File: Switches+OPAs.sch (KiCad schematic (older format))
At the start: 23 parts, among them J15 Screw_Terminal_01x03, SW1 SW_Rotary2x6, SW2 SW_Rotary2x6, SW3 SW_Rotary2x6, SW4 SW_Rotary2x6, SW5 SW_Rotary2x6, SW6 SW_Rotary2x6, U1 TL072, U2 TL072, U3 TL072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

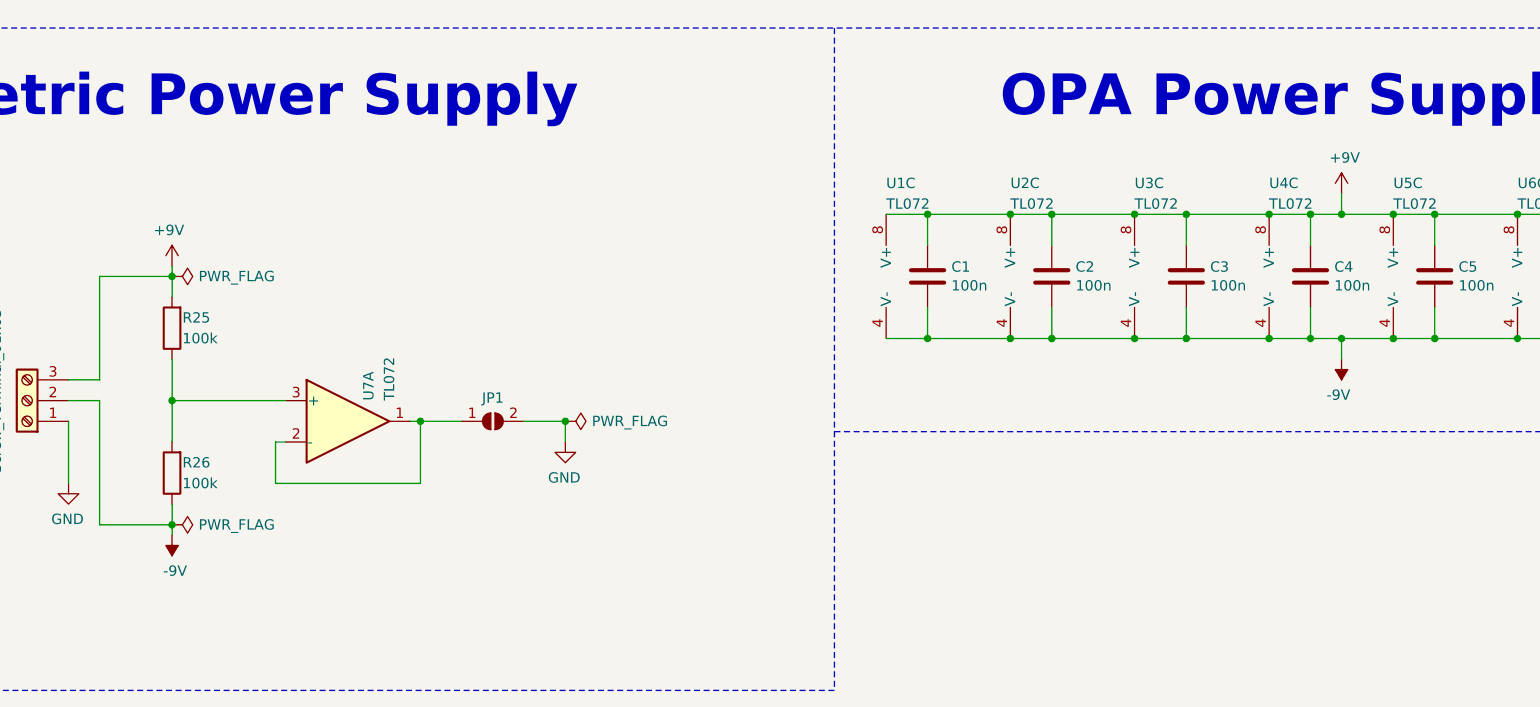
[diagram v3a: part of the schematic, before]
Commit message: added new attributes MF, MFN, Mouser, Digi-Key, RS-Online, Infopage, datasheet | bill of material (BOM) created | infobox updated | added AudioBürokrat logo on silkscreen
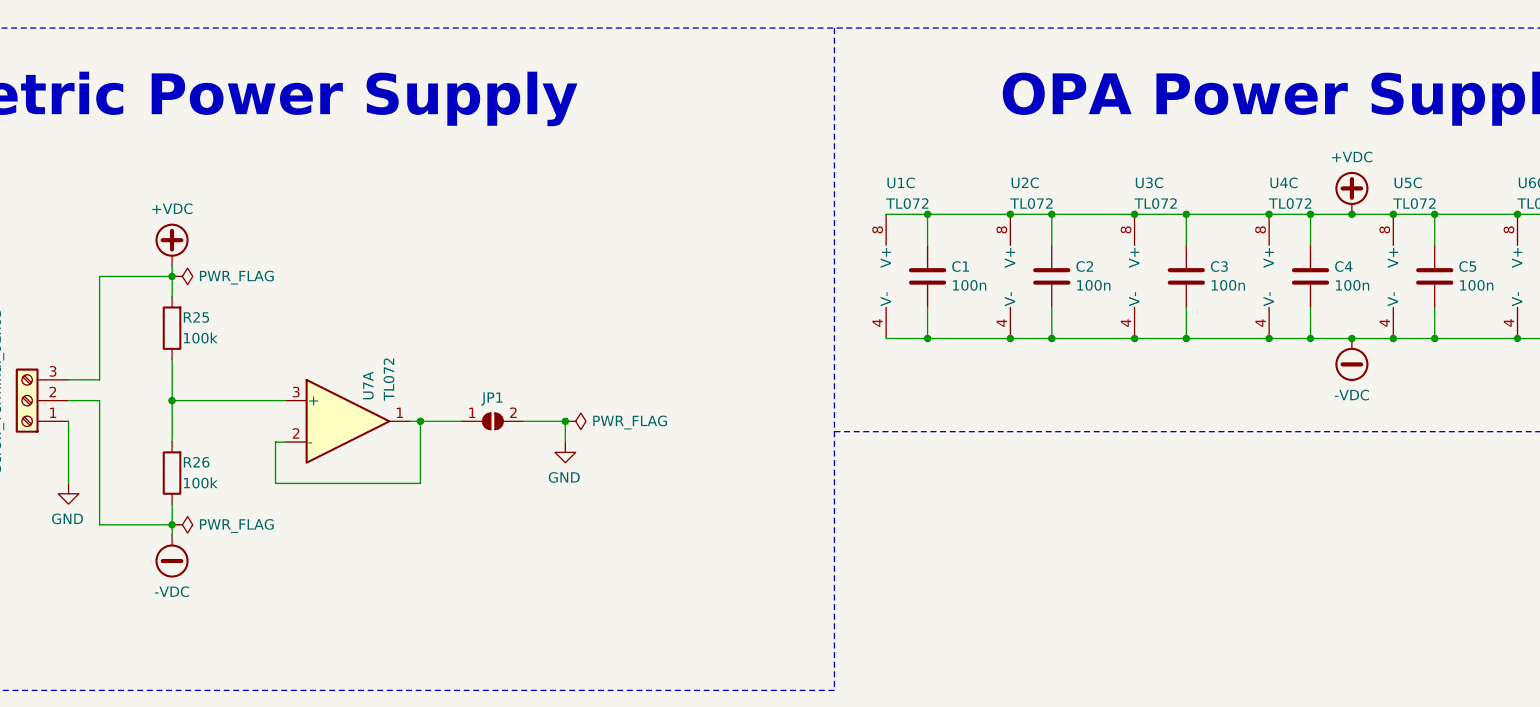
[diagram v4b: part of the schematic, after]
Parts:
- C1, C2, C3, C4, C5, C6: Digi-Key (none) -> 311-1779-1-ND; Infopage (none) -> —; MF (none) -> Yageo; MFN (none) -> CC0603JRX7R9BB104; Mouser (none) -> 603-CC603JRX7R9BB104; RS-Online (none) -> 200-6519
- J15: Digi-Key (none) -> 732-2029-ND; Infopage (none) -> https://www.we-online.de/katalog/de/TBL_5_00_102_6911027100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; MF (none) -> Wuerth; MFN (none) -> 691102710003; Mouser (none) -> 710-691102710003; RS-Online (none) -> 691102710003
- JP1: Digi-Key (none) -> —; Infopage (none) -> —; MF (none) -> —; MFN (none) -> —; Mouser (none) -> —; RS-Online (none) -> —
- R25, R26: Digi-Key (none) -> 541-3950-1-ND; Infopage (none) -> —; MF (none) -> Vishay; MFN (none) -> CRCW0603100KFKEAC; Mouser (none) -> 71-CRCW0603100KFKEAC; RS-Online (none) -> 820-6745
- SW1, SW2, SW3, SW4, SW5, SW6: Digi-Key (none) -> —; Infopage (none) -> https://lorlinelectronics.co.uk/product/ck; MF (none) -> Lorlin; MFN (none) -> CK1050; Mouser (none) -> —; RS-Online (none) -> 665-196
- U1, U2, U3, U4, U5, U6, U7: Digi-Key (none) -> 296-1282-2-ND; Infopage (none) -> https://www.ti.com/store/ti/en/p/product/?p=TL072CDR; MF (none) -> TI; MFN (none) -> TL072CDR; Mouser (none) -> 595-TL072CDR; RS-Online (none) -> 197-7552
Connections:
- net +9V renamed +VDC
- net -9V renamed -VDC
